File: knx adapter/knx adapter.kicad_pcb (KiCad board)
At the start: 2 copper layers, 40 x 22 mm, 5 parts, among them J1 Conn_02x05_Odd_Even, J2 Conn_02x05_Odd_Even

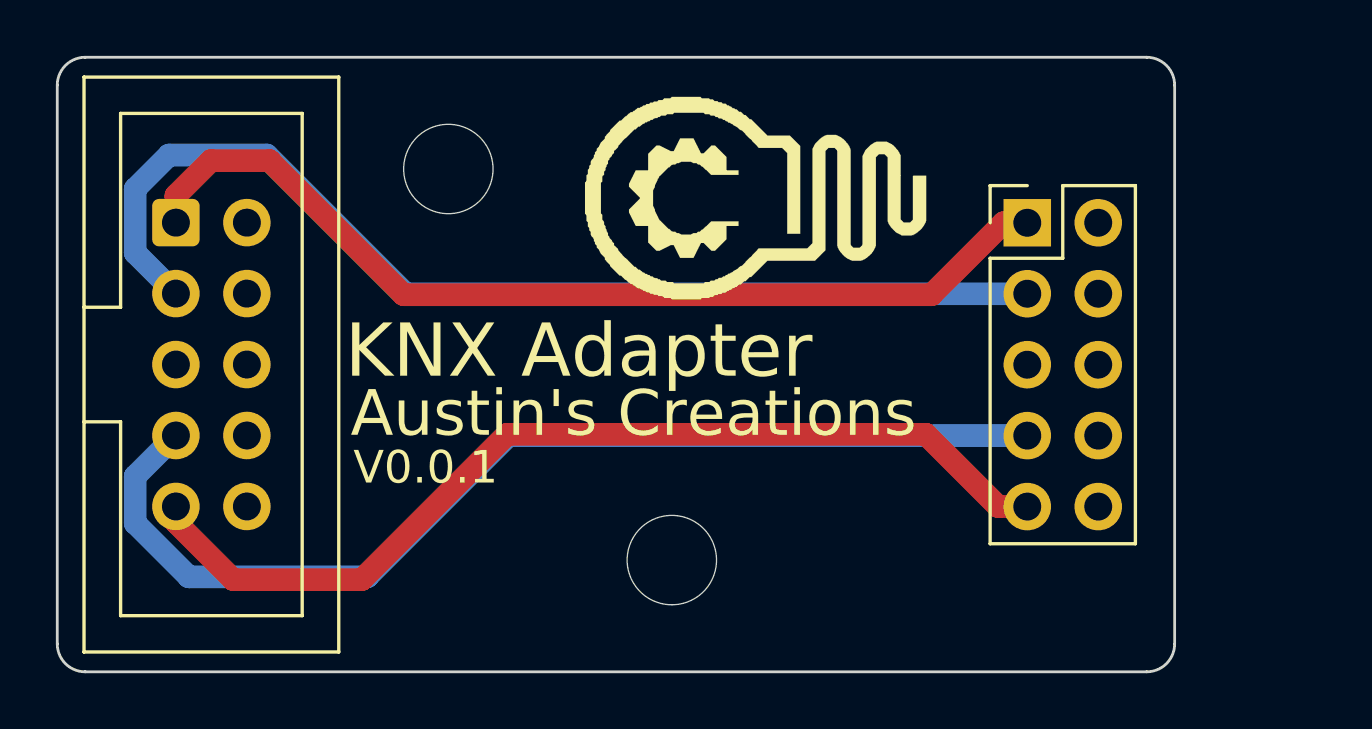
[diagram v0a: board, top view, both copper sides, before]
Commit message: update adapter to rev 002
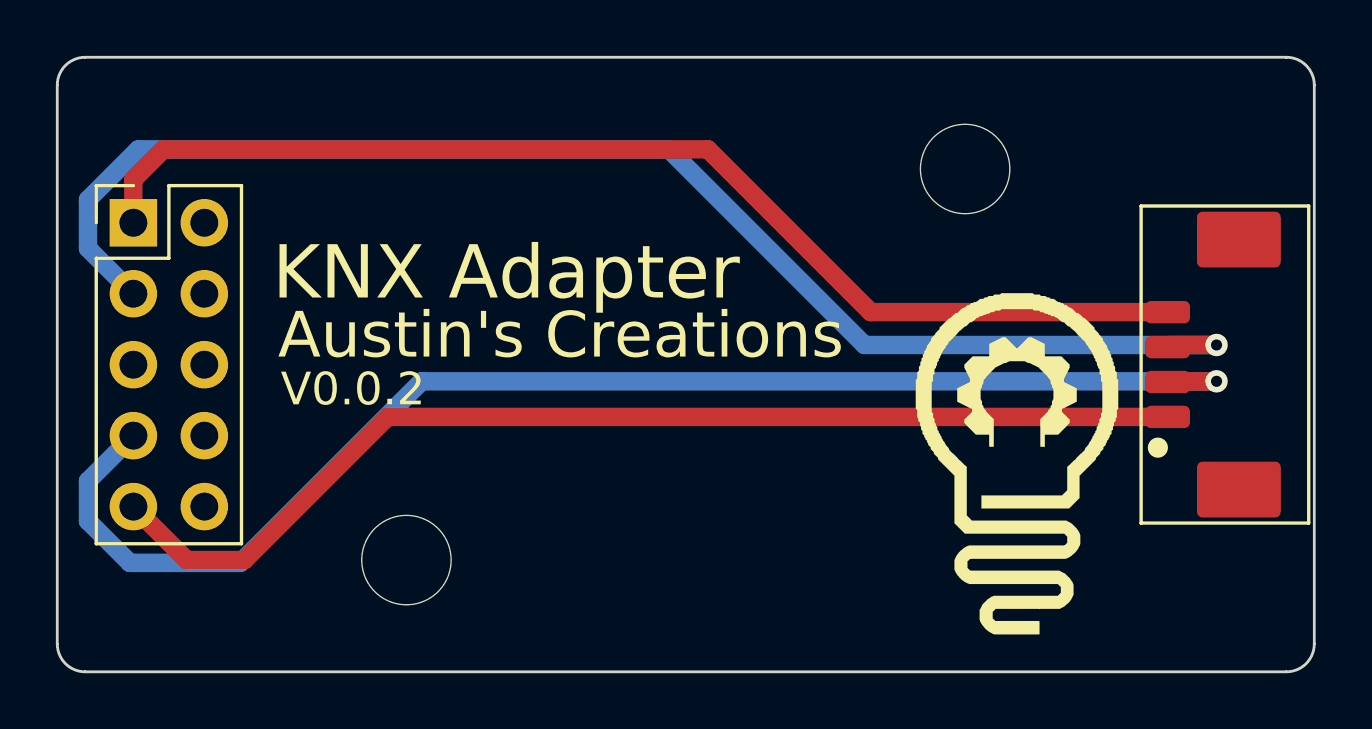
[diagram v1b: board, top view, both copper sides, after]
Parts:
- J2: value Conn_02x05_Odd_Even -> KNX; footprint Connector_IDC:IDC-Header_2x05_P2.54mm_Vertical -> bare-footprints:4 pin jst 1.25 horizontal
- moved J2 38.4 mm to (62.3, 31.0), turned to 90 degrees
- moved J1 32.0 mm to (22.7, 25.9)
- moved H2 18.5 mm to (52.5, 24.0), turned to 180 degrees
- moved LOGO1 13.8 mm to (54.4, 32.1), turned to 0 degrees
- moved H1 9.50 mm to (32.5, 38.0), turned to 180 degrees
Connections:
- J1 pad 1: KNX GND -> KNX_5V
- J1 pad 3: KNX_RX -> KNX_TX
- J1 pad 7: KNX_TX -> KNX_RX
- J1 pad 9: KNX_5V -> KNX GND
- J2 pad 2: unconnected-(J2-Pad2) -> KNX_RX
- J2 pad 3: KNX_RX -> KNX_TX
- J2 pad 4: unconnected-(J2-Pad4) -> KNX_5V
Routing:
- net KNX_TX: track 38.6 -> 49.9 mm, vias 0 -> 1
- net KNX_RX: track 38.8 -> 49.2 mm, vias 0 -> 1
- net KNX_5V: track 35.1 -> 41.4 mm
- net KNX GND: track 35.0 -> 39.9 mm
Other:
- board size 40 x 22 mm -> 45 x 22 mm
- board text added: "V0.0.2"
- board text removed: "V0.0.1"
